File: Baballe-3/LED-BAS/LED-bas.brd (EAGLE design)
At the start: 46.2 x 46.2 mm, 23 parts, among them Q1 200mA/50V, Q2 200mA/50V, Q3 200mA/50V, Q4 200mA/50V

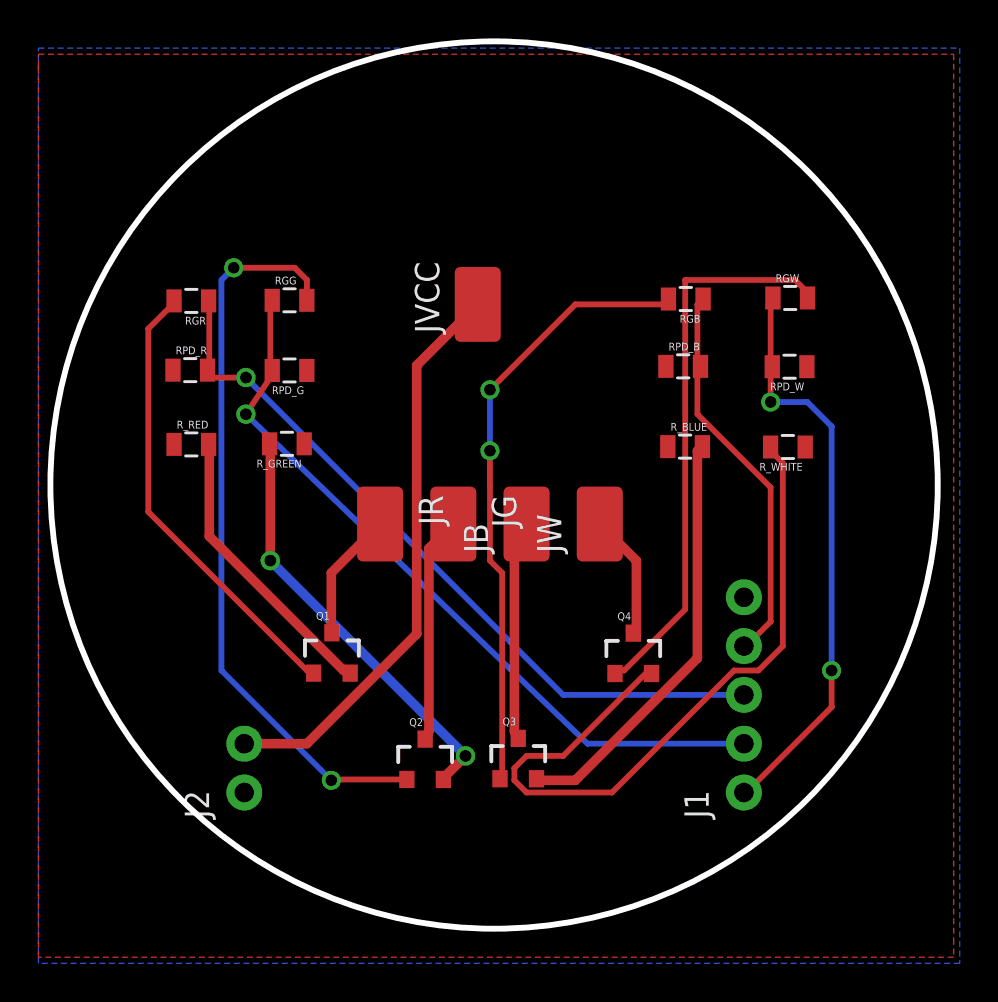
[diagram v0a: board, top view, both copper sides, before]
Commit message: Patch height error
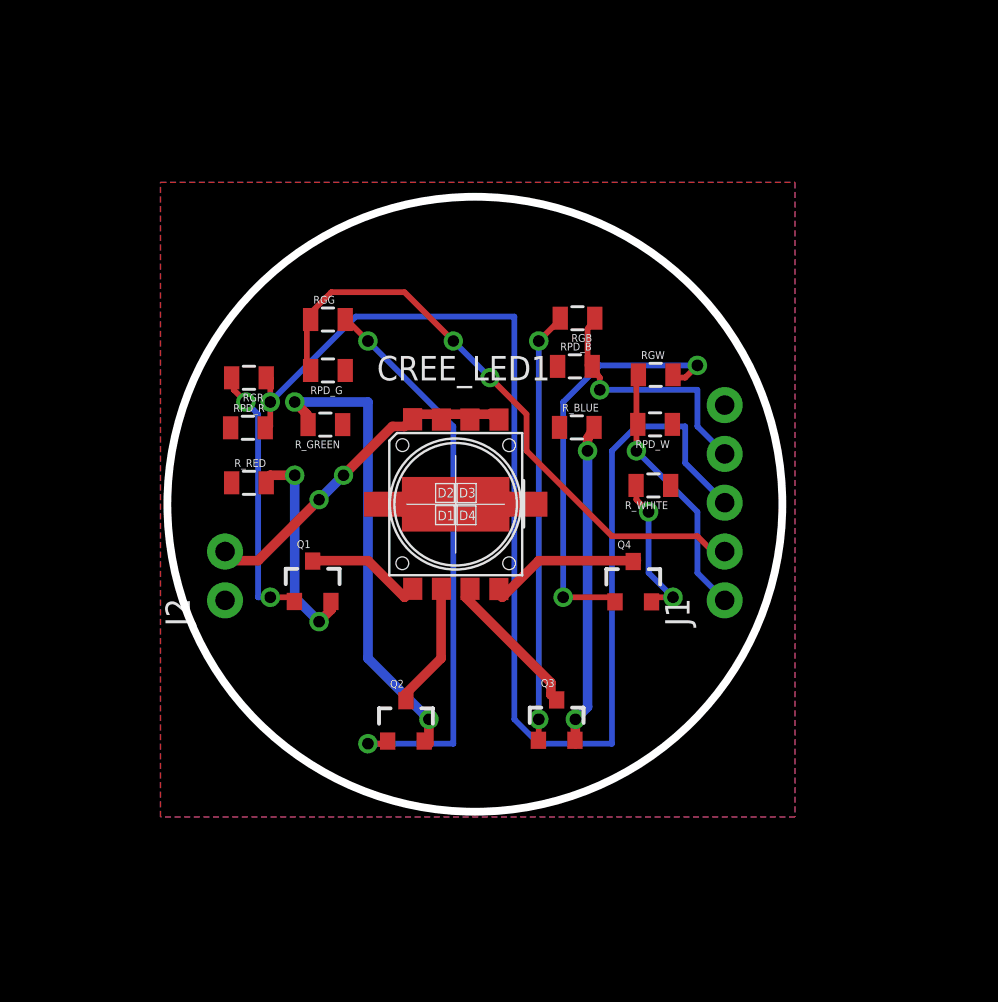
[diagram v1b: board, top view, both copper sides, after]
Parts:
- removed JB, JG, JR, JVCC, JW: (no value), SparkFun-Connectors:LUXEON-PAD
- added CREE_LED1: CREE_XL_MCE, CreeXL-MC-E:CREE_XL_MCE
- moved J1 10.0 mm to (70.0, 10.0)
- moved J2 10.0 mm to (44.0, 10.0)
- moved RGW 8.06 mm to (66.4, 21.7)
- moved RPD_W 7.62 mm to (66.4, 19.2)
- moved R_WHITE 7.28 mm to (66.3, 16.0)
- moved R_BLUE 5.72 mm to (62.3, 19.0)
- moved RGB 5.72 mm to (62.3, 24.7)
- moved RPD_B 5.64 mm to (62.2, 22.2)
- moved RGR 5.00 mm to (45.2, 21.6)
- moved RPD_R 4.24 mm to (45.2, 19.0)
- moved Q1 3.86 mm to (48.6, 10.9)
- moved Q4 3.73 mm to (65.2, 10.9)
- moved R_RED 3.61 mm to (45.2, 16.1)
- moved Q3 2.83 mm to (61.3, 3.72)
- moved Q2 2.24 mm to (53.4, 3.68)
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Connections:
- net N$10: now also CREE_LED1.8; no longer JR.P$1
- net N$11: now also CREE_LED1.7; no longer JG.P$1
- net N$14: now also CREE_LED1.5; no longer JW.P$1
- net N$9: now also CREE_LED1.6; no longer JB.P$1
- net VCC: now also CREE_LED1.1, CREE_LED1.2, CREE_LED1.3, CREE_LED1.4; no longer JVCC.P$1
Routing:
- net O_RED: track 38.7 -> 68.5 mm
- net N$8: track 38.0 -> 8.16 mm, vias 0 -> 2
- net O_WHITE: track 30.3 -> 13.7 mm, vias 2 -> 1
- net VCC: track 29.8 -> 18.2 mm, vias 0 -> 2
- net N$5: track 23.6 -> 14.2 mm, vias 0 -> 2
- net N$6: track 32.5 -> 23.1 mm
- net N$4: track 38.4 -> 30.3 mm
- net O_BLUE: track 20.6 -> 13.2 mm, vias 0 -> 1
- net N$13: track 29.4 -> 22.4 mm, vias 0 -> 2
- net O_GREEN: track 39.2 -> 32.5 mm, vias 1 -> 2
- net N$1: track 22.2 -> 17.0 mm, vias 0 -> 2
- net N$11: track 11.8 -> 6.62 mm
- net N$3: track 15.0 -> 11.2 mm, vias 0 -> 2
- net N$9: track 11.5 -> 7.82 mm
- net N$2: track 22.4 -> 24.6 mm
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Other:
- board size 46.2 x 46.2 mm -> 32 x 32 mm
